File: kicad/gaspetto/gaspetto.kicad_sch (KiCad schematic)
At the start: 6 parts, among them U1 BP, U2 A1369xUA-10, U3 A1369xUA-10, U4 A1369xUA-10, U5 A1369xUA-10, U7 nRF24L01+

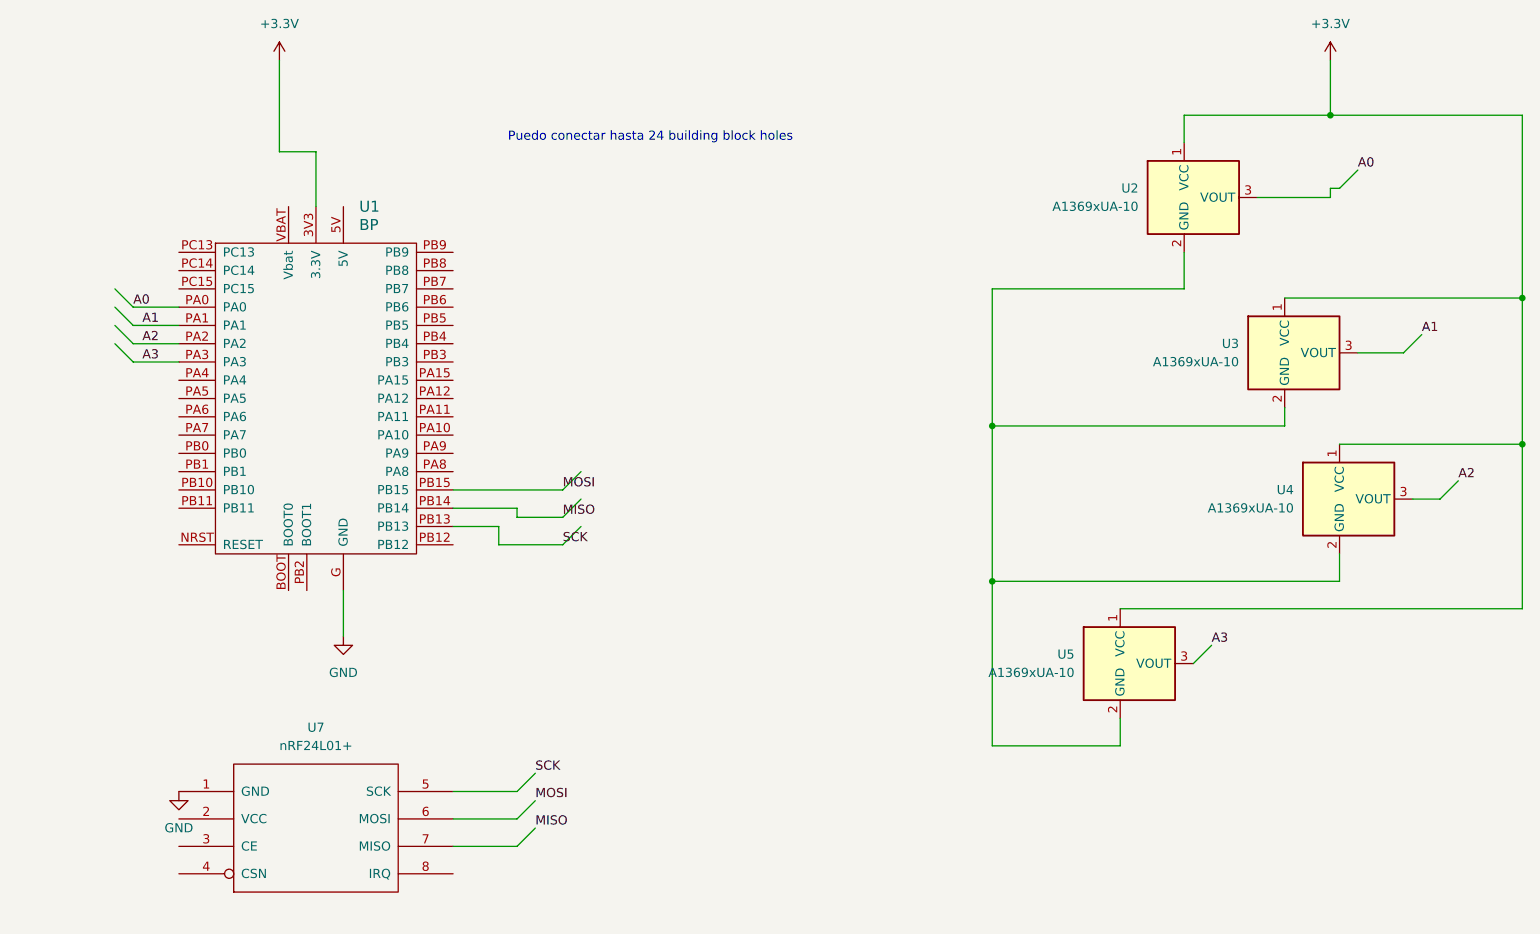
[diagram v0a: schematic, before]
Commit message: kicad: add gaspetto schematic + kicad libs
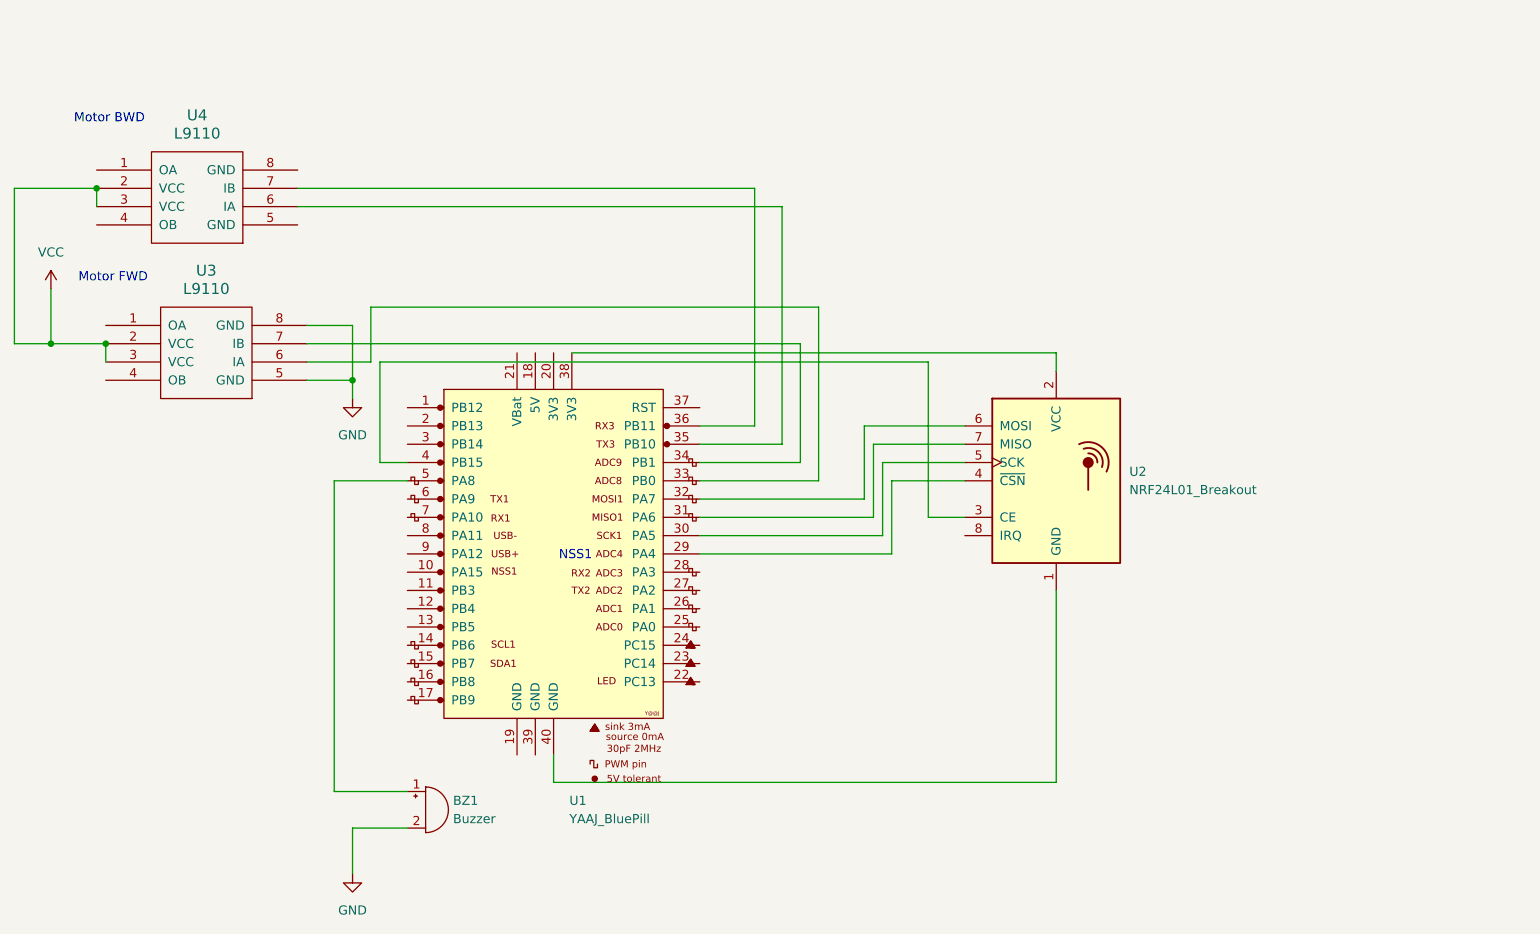
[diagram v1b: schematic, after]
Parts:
- removed U1: BP, Module:blue_pill, symbol bluepill:BP
- removed U2, U3, U4, U5: A1369xUA-10, Sensor_Current:Allegro_SIP-3, symbol Sensor_Current:A1369xUA-10
- removed U7: nRF24L01+, MODULE, symbol nRF24L01+:nRF24L01+
- added BZ1: Buzzer, symbol Device:Buzzer
- added U1: YAAJ_BluePill, symbol YAAJ_BluePill:YAAJ_BluePill
- added U2: NRF24L01_Breakout, RF_Module:nRF24L01_Breakout, symbol RF:NRF24L01_Breakout
- added U3, U4: L9110, symbol L9110:L9110
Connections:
- net GND: now also BZ1.2 (-), U3.5 (GND), U3.8 (GND)
- new net: U1.33 (PB0), U3.6 (IA)
- new net: U1.34 (PB1), U3.7 (IB)
- new net: BZ1.1 (+), U1.5 (PA8)
- new net: U1.29 (PA4), U2.4 (~{CSN})
- new net: U1.30 (PA5), U2.5 (SCK)
- new net: U1.31 (PA6), U2.7 (MISO)
- new net: U1.32 (PA7), U2.6 (MOSI)
- new net: U1.35 (PB10), U4.6 (IA)
- new net: U1.36 (PB11), U4.7 (IB)
- new net: U1.38 (3V3), U2.2 (VCC)
- new net: U1.4 (PB15), U2.3 (CE)
- new net: U1.40 (GND), U2.1 (GND)
- new net VCC: U3.2 (VCC), U3.3 (VCC), U4.2 (VCC), U4.3 (VCC)
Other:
- note added: "Motor BWD"
- note added: "Motor FWD"
- note added: "NSS1"
- note removed: "Puedo conectar hasta 24 building block holes"
